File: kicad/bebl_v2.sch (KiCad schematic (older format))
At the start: 51 parts, among them P1 ISP, P2 FTDI, P3 LED_1, P4 LED_2, P5 LED_3, P6 LED_PWR, P7 USB-Micro, P8 CHG_LED, P9 Ext_LiPo, SW1 RST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

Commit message: track layout done. Needs verification
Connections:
- net LED_D3: now reaches P4.1 (P1)
- net LED_D3: now also U1.11 (PD7(AIN1)); no longer U1.10 (PD6(AIN0))
- net LED_B6: now reaches P5.2 (PM)
- net LED_B6: now also P1.3, U1.17 (PB5(SCK)); no longer U1.11 (PD7(AIN1))
- net LED_P4: now reaches P4.2 (PM), U1.13 (PB1(OC1A))
- net LED_P1: now reaches U1.9 (PD5(T1))
- net LED_P1: now also P3.1 (P1); no longer P3.2 (PM)
- net LED_K: now reaches P8.2 (PM), R5.1
- removed net SCK: P1.3, P3.1 (P1), U1.17 (PB5(SCK))
- net SS renamed LED_P5
- new net LED_P2: P3.2 (PM), U1.10 (PD6(AIN0))
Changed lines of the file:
@@
 	3450 4450 3400 4450
 Wire Wire Line
-	3400 4550 4200 4550
+	3400 4550 3700 4550
 Wire Wire Line
 	1500 2450 1300 2450
@@
 $EndComp
 Wire Wire Line
-	3400 4250 3975 4250
+	3400 4250 3700 4250
 $Comp
 L PWR_FLAG #FLG07
@@
 ACL_INT2
 Wire Wire Line
-	4800 3750 4200 3750
-Wire Wire Line
-	4200 3750 4200 4550
-Wire Wire Line
-	3400 3650 4125 3650
-Wire Wire Line
-	4125 3650 4125 3950
-Wire Wire Line
-	4125 3950 4800 3950
-Wire Wire Line
-	3400 3750 4075 3750
-Wire Wire Line
-	4075 3750 4075 4100
-Wire Wire Line
-	4075 4100 4800 4100
-Wire Wire Line
-	3400 4150 4025 4150
-Wire Wire Line
-	4025 4150 4025 4300
-Wire Wire Line
-	4025 4300 4800 4300
-Wire Wire Line
-	3975 4250 3975 4450
-Wire Wire Line
-	3975 4450 4800 4450
+	4800 4650 3700 4650
+Wire Wire Line
+	3700 4650 3700 4550
+Wire Wire Line
+	3400 3650 4100 3650
+Wire Wire Line
+	4100 3650 4100 3750
+Wire Wire Line
+	4100 3750 4800 3750
+Wire Wire Line
+	3400 3750 4000 3750
+Wire Wire Line
+	4000 3750 4000 3950
+Wire Wire Line
+	4000 3950 4800 3950
+Wire Wire Line
+	3400 4150 3800 4150
+Wire Wire Line
+	3800 4150 3800 4300
+Wire Wire Line
+	3800 4300 4800 4300
+Wire Wire Line
+	3700 4250 3700 4450
+Wire Wire Line
+	3700 4450 4800 4450
 $Comp
 L I/O B7
@@
 $EndComp
 Wire Wire Line
-	3400 3850 3925 3850
-Wire Wire Line
-	3925 3850 3925 4650
-Wire Wire Line
-	3925 4650 4800 4650
+	3400 3850 3900 3850
+Wire Wire Line
+	3900 3850 3900 4100
+Wire Wire Line
+	3900 4100 4800 4100
 $Sheet
 S 4550 6850 2300 750
@@
 Text Label 4650 5000 0    50   ~ 0
 GND
+Text Label 4200 3750 0    39   ~ 0
+LED_P1
+Text Label 4200 3950 0    39   ~ 0
+LED_P2
+Text Label 4200 4100 0    39   ~ 0
+LED_D3
+Text Label 4200 4300 0    39   ~ 0
+LED_P4
+Text Label 4200 4450 0    39   ~ 0
+LED_P5
+Text Label 4200 4650 0    39   ~ 0
+LED_B6
+Text Label 9050 2225 0    39   ~ 0
+LED_K
 $EndSCHEMATC

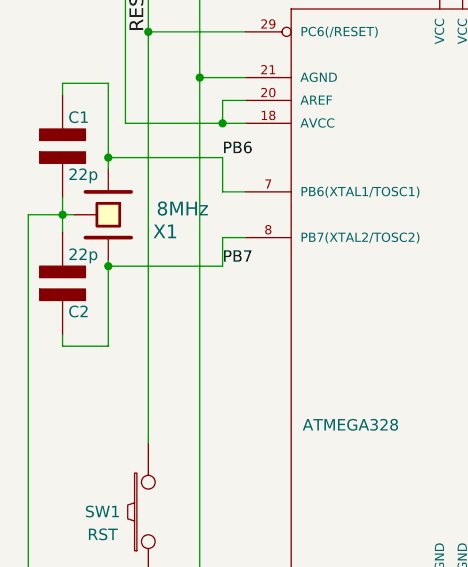
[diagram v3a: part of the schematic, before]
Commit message: DFM changes to bebl_v2 based on seeed feedback
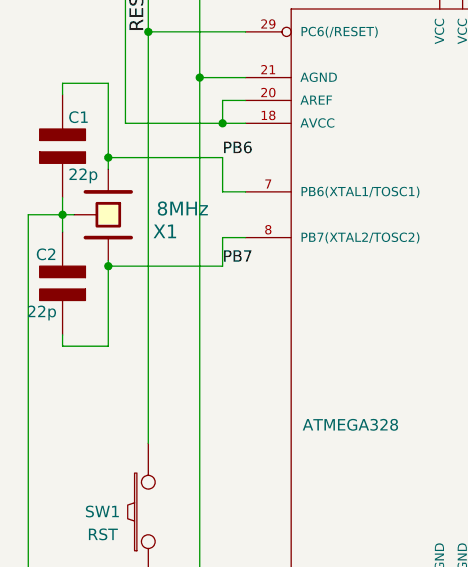
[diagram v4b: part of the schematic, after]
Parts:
- P7: footprint bebl_v2_pretty:USB_B_Micro -> bebl_v2_pretty:USB_B_Micro_seeed
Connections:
- net GND: now also C2.2; no longer C2.1
- net PB7: now also C2.1; no longer C2.2
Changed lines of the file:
@@
 F 4 "490-1734-1-ND" H 700 3550 60  0001 C CNN "Digikey"
 	1    700  3350
-	1    0    0    -1
+	-1   0    0    1
 $EndComp
 $Comp
@@
 F 0 "P7" H 7075 1425 50  0000 C CNN
 F 1 "USB-Micro" H 6925 1350 50  0000 C CNN
-F 2 "bebl_v2_pretty:USB_B_Micro" H 7650 1350 60  0001 C CNN
+F 2 "bebl_v2_pretty:USB_B_Micro_seeed" H 7650 1350 60  0001 C CNN
 F 3 "" H 7650 1350 60  0000 C CNN
 	1    7650 1350
